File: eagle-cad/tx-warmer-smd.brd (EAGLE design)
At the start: 28.6 x 19 mm, 27 parts, among them Q1 MOSFET-NCHANNELFDS6630A, U2 V_REG_LDOSMD

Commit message: Minor updates to SMD-version
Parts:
- Q1: value MOSFET-NCHANNELFDS6630A -> IR F8721
- U2: value V_REG_LDOSMD -> MCP1804T
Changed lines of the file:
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@@
 <attribute name="VALUE" x="12.827" y="20.574" size="0.4064" layer="25" rot="R90"/>
 </element>
-<element name="Q1" library="SparkFun-DiscreteSemi" package="SO08" value="MOSFET-NCHANNELFDS6630A" x="7.62" y="21.59" smashed="yes">
+<element name="Q1" library="SparkFun-DiscreteSemi" package="SO08" value="IR F8721" x="7.62" y="21.59" smashed="yes">
 <attribute name="PROD_ID" value="IC-08089" x="7.62" y="21.59" size="1.778" layer="27" display="off"/>
 </element>
@@
 <attribute name="VALUE" x="10.287" y="14.224" size="0.4064" layer="25" rot="R90"/>
 </element>
-<element name="U2" library="SparkFun-PowerIC" package="SOT23-5" value="V_REG_LDOSMD" x="10.16" y="11.43" smashed="yes" rot="R270"/>
+<element name="U2" library="SparkFun-PowerIC" package="SOT23-5" value="MCP1804T" x="10.16" y="11.43" smashed="yes" rot="R270"/>
 <element name="S1" library="SparkFun-Electromechanical" package="TACTILE_SWITCH_SMD" value="" x="24.13" y="21.59" smashed="yes">
 <attribute name="PROD_ID" value="SWCH-08247" x="24.13" y="21.59" size="1.778" layer="27" display="off"/>

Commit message: Fixed ldo shutdown-pin and checked values for res/caps
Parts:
- C1, C3: value 2.2uF? -> 1uF
- C2: value 22uF? -> 10uF
- R1: value 270? -> 270
- R5: value 220? -> 220
- R6: value 270? -> 100k
- R8: value 270? -> 33k
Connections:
- net GND: no longer U2.4
- net VIN: now also U2.4
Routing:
- net VIN: track 17.8 -> 21.2 mm
- net GND: vias 0 -> 8
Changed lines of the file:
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@@
 <attribute name="VALUE" x="17.907" y="10.414" size="0.4064" layer="25" rot="R90"/>
 </element>
-<element name="R1" library="SparkFun-Resistors" package="0805" value="270?" x="25.4" y="16.51" smashed="yes" rot="R270">
+<element name="R1" library="SparkFun-Resistors" package="0805" value="270" x="25.4" y="16.51" smashed="yes" rot="R270">
 <attribute name="VALUE" x="24.003" y="17.526" size="0.4064" layer="25" rot="R270"/>
 </element>
-<element name="R5" library="SparkFun-Resistors" package="0805" value="220?" x="22.225" y="16.51" smashed="yes" rot="R270">
+<element name="R5" library="SparkFun-Resistors" package="0805" value="220" x="22.225" y="16.51" smashed="yes" rot="R270">
 <attribute name="VALUE" x="20.828" y="17.526" size="0.4064" layer="25" rot="R270"/>
 </element>
@@
 <attribute name="NAME" x="0.7112" y="22.1488" size="1.016" layer="25" rot="R90"/>
 </element>
-<element name="C3" library="SparkFun-Capacitors" package="0805" value="2.2uF?" x="6.35" y="11.43" smashed="yes" rot="R270">
+<element name="C3" library="SparkFun-Capacitors" package="0805" value="1uF" x="6.35" y="11.43" smashed="yes" rot="R270">
 <attribute name="VALUE" x="5.207" y="10.414" size="0.4064" layer="25" rot="R90"/>
 </element>
-<element name="C1" library="SparkFun-Capacitors" package="0805" value="2.2uF?" x="13.97" y="11.43" smashed="yes" rot="R270">
+<element name="C1" library="SparkFun-Capacitors" package="0805" value="1uF" x="13.97" y="11.43" smashed="yes" rot="R270">
 <attribute name="VALUE" x="12.827" y="10.414" size="0.4064" layer="25" rot="R90"/>
 </element>
-<element name="C2" library="SparkFun-Capacitors" package="0805" value="22uF?" x="16.51" y="11.43" smashed="yes" rot="R270">
+<element name="C2" library="SparkFun-Capacitors" package="0805" value="10uF" x="16.51" y="11.43" smashed="yes" rot="R270">
 <attribute name="VALUE" x="15.367" y="10.414" size="0.4064" layer="25" rot="R90"/>
 </element>
-<element name="R6" library="SparkFun-Resistors" package="0805" value="270?" x="6.35" y="15.24" smashed="yes" rot="R270">
+<element name="R6" library="SparkFun-Resistors" package="0805" value="100k" x="6.35" y="15.24" smashed="yes" rot="R270">
 <attribute name="VALUE" x="5.207" y="14.224" size="0.4064" layer="25" rot="R90"/>
 </element>
-<element name="R8" library="SparkFun-Resistors" package="0805" value="270?" x="8.89" y="15.24" smashed="yes" rot="R90">
+<element name="R8" library="SparkFun-Resistors" package="0805" value="33k" x="8.89" y="15.24" smashed="yes" rot="R90">
 <attribute name="VALUE" x="7.747" y="14.224" size="0.4064" layer="25" rot="R90"/>
 </element>
@@
 <contactref element="R8" pad="1"/>
 <contactref element="C5" pad="2"/>
-<contactref element="U2" pad="4"/>
 <contactref element="U2" pad="2"/>
 <polygon width="0.508" layer="1" isolate="0.3048">
@@
 <vertex x="-1.905" y="6.985"/>
 </polygon>
+<via x="13.97" y="13.97" extent="1-16" drill="0.6"/>
+<via x="10.795" y="19.05" extent="1-16" drill="0.6"/>
+<via x="26.035" y="25.4" extent="1-16" drill="0.6"/>
+<via x="5.08" y="9.525" extent="1-16" drill="0.6"/>
+<via x="7.62" y="9.525" extent="1-16" drill="0.6"/>
+<via x="12.7" y="9.525" extent="1-16" drill="0.6"/>
+<via x="17.78" y="9.525" extent="1-16" drill="0.6"/>
+<via x="23.8125" y="9.525" extent="1-16" drill="0.6"/>
 </signal>
 <signal name="5V">
@@
 <wire x1="6.35" y1="12.7" x2="6.35" y2="13.335" width="0.6096" layer="1"/>
 <wire x1="6.35" y1="13.97" x2="5.715" y2="13.335" width="0.6096" layer="1"/>
+<contactref element="U2" pad="4"/>
+<wire x1="8.8599" y1="12.38" x2="9.21" y2="12.38" width="0.4064" layer="1"/>
+<wire x1="9.21" y1="12.38" x2="11.11" y2="10.48" width="0.4064" layer="1"/>
+<wire x1="11.4601" y1="10.48" x2="11.11" y2="10.48" width="0.4064" layer="1"/>
 </signal>
 <signal name="N$3">

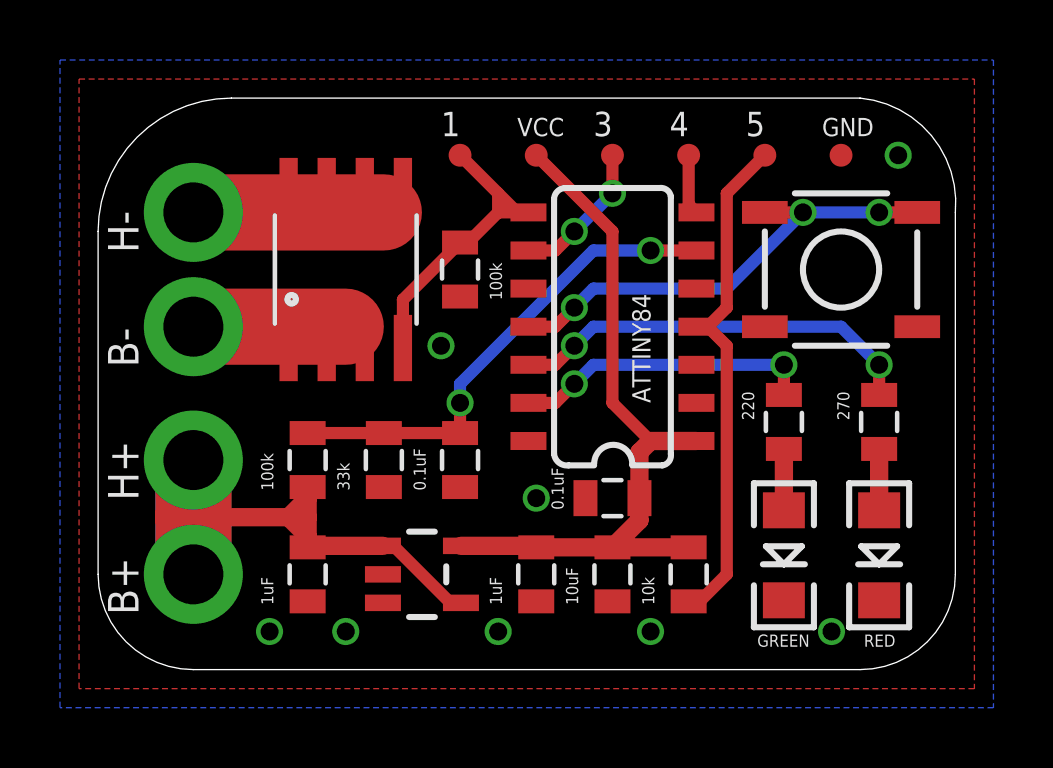
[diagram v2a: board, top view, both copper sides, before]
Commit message: Added top gnd-plane
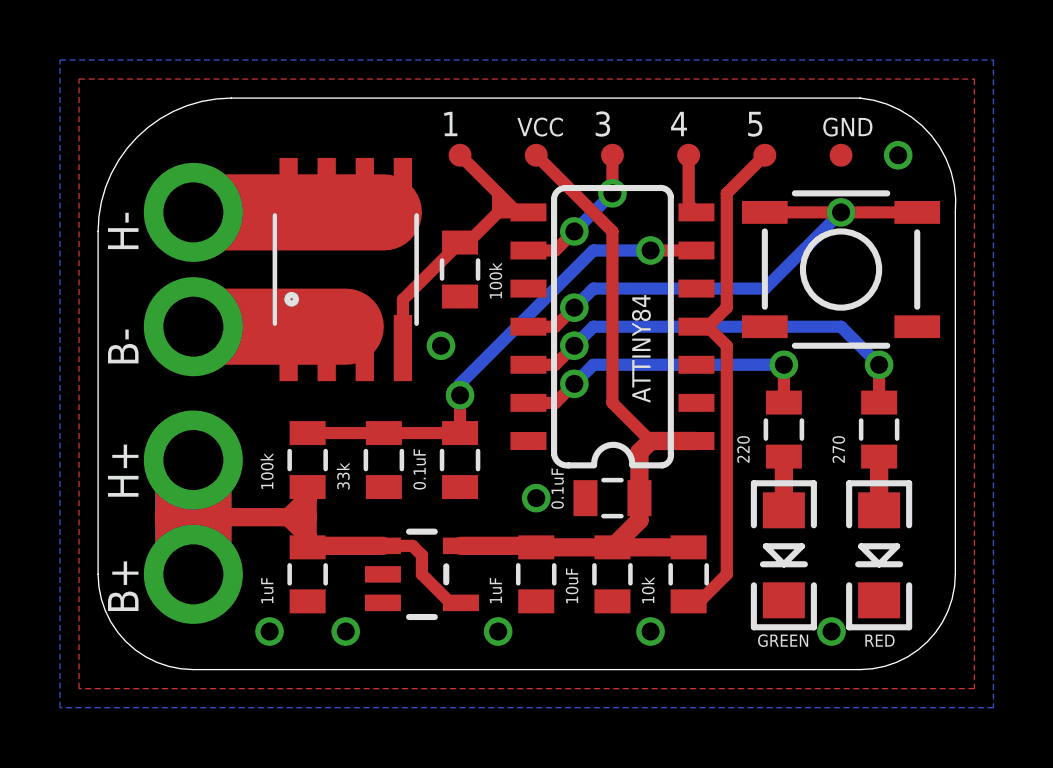
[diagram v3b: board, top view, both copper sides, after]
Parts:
- moved R1 0.25 mm to (25.4, 16.3)
- moved R5 0.25 mm to (22.2, 16.3)
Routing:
- net N$1: track 15.8 -> 17.1 mm, vias 3 -> 2
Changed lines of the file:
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@@
 </class>
 </classes>
-<designrules name="ITEADstudio_DRC">
+<designrules name="LaenPCBOrder">
 <description language="de">&lt;b&gt;EAGLE Design Rules&lt;/b&gt;
 &lt;p&gt;
@@
 Einstellungen hier und speichern die Design Rules unter
 einem neuen Namen ab.</description>
-<description language="en">&lt;b&gt;EAGLE Design Rules&lt;/b&gt;
+<description language="en">&lt;b&gt;Laen's PCB Order Design Rules&lt;/b&gt;
 &lt;p&gt;
-The default Design Rules have been set to cover
-a wide range of applications. Your particular design
-may have different requirements, so please make the
-necessary adjustments and save your customized
-design rules under a new name.</description>
-<description language="zh">&lt;b&gt;Seeed Studio EAGLE Design Rules&lt;/b&gt;
-</description>
+Please make sure your boards conform to these design rules.</description>
 <param name="layerSetup" value="(1*16)"/>
-<param name="mtCopper" value="0.035mm 0.035mm 0.035mm 0.035mm 0.035mm 0.035mm 0.035mm 0.035mm 0.035mm 0.035mm 0.035mm 0.035mm 0.035mm 0.035mm 0.035mm 0.035mm"/>
-<param name="mtIsolate" value="1.5mm 0.15mm 0.2mm 0.15mm 0.2mm 0.15mm 0.2mm 0.15mm 0.2mm 0.15mm 0.2mm 0.15mm 0.2mm 0.15mm 0.2mm"/>
+<param name="mtCopper" value="0.0356mm 0.0356mm 0.0356mm 0.0356mm 0.0356mm 0.0356mm 0.0356mm 0.0356mm 0.0356mm 0.0356mm 0.0356mm 0.0356mm 0.0356mm 0.0356mm 0.0356mm 0.0356mm"/>
+<param name="mtIsolate" value="1.5011mm 0.1499mm 0.2007mm 0.1499mm 0.2007mm 0.1499mm 0.2007mm 0.1499mm 0.2007mm 0.1499mm 0.2007mm 0.1499mm 0.2007mm 0.1499mm 0.2007mm"/>
 <param name="mdWireWire" value="6mil"/>
 <param name="mdWirePad" value="6mil"/>
@@
 <param name="mdPadVia" value="6mil"/>
 <param name="mdViaVia" value="6mil"/>
-<param name="mdSmdPad" value="0mil"/>
-<param name="mdSmdVia" value="0mil"/>
-<param name="mdSmdSmd" value="0mil"/>
+<param name="mdSmdPad" value="6mil"/>
+<param name="mdSmdVia" value="6mil"/>
+<param name="mdSmdSmd" value="6mil"/>
 <param name="mdViaViaSameLayer" value="8mil"/>
 <param name="mnLayersViaInSmd" value="2"/>
-<param name="mdCopperDimension" value="10mil"/>
-<param name="mdDrill" value="10mil"/>
+<param name="mdCopperDimension" value="15mil"/>
+<param name="mdDrill" value="6mil"/>
 <param name="mdSmdStop" value="0mil"/>
 <param name="msWidth" value="6mil"/>
-<param name="msDrill" value="12mil"/>
-<param name="msMicroVia" value="12mil"/>
+<param name="msDrill" value="13mil"/>
+<param name="msMicroVia" value="13mil"/>
 <param name="msBlindViaRatio" value="0.5"/>
 <param name="rvPadTop" value="0.25"/>
@@
 <param name="rvMicroViaOuter" value="0.25"/>
 <param name="rvMicroViaInner" value="0.25"/>
-<param name="rlMinPadTop" value="10mil"/>
+<param name="rlMinPadTop" value="7mil"/>
 <param name="rlMaxPadTop" value="20mil"/>
-<param name="rlMinPadInner" value="10mil"/>
+<param name="rlMinPadInner" value="7mil"/>
 <param name="rlMaxPadInner" value="20mil"/>
-<param name="rlMinPadBottom" value="10mil"/>
+<param name="rlMinPadBottom" value="7mil"/>
 <param name="rlMaxPadBottom" value="20mil"/>
-<param name="rlMinViaOuter" value="6mil"/>
+<param name="rlMinViaOuter" value="7mil"/>
 <param name="rlMaxViaOuter" value="20mil"/>
-<param name="rlMinViaInner" value="6mil"/>
+<param name="rlMinViaInner" value="7mil"/>
 <param name="rlMaxViaInner" value="20mil"/>
 <param name="rlMinMicroViaOuter" value="4mil"/>
@@
 <param name="psTop" value="-1"/>
 <param name="psBottom" value="-1"/>
-<param name="psFirst" value="0"/>
+<param name="psFirst" value="-1"/>
 <param name="psElongationLong" value="100"/>
 <param name="psElongationOffset" value="100"/>
 <param name="mvStopFrame" value="1"/>
 <param name="mvCreamFrame" value="0"/>
-<param name="mlMinStopFrame" value="2mil"/>
-<param name="mlMaxStopFrame" value="2mil"/>
+<param name="mlMinStopFrame" value="4mil"/>
+<param name="mlMaxStopFrame" value="4mil"/>
 <param name="mlMinCreamFrame" value="0mil"/>
 <param name="mlMaxCreamFrame" value="0mil"/>
-<param name="mlViaStopLimit" value="100mil"/>
+<param name="mlViaStopLimit" value="0mil"/>
 <param name="srRoundness" value="0"/>
 <param name="srMinRoundness" value="0mil"/>
@@
 <param name="checkAngle" value="0"/>
 <param name="checkFont" value="1"/>
-<param name="checkRestrict" value="0"/>
+<param name="checkRestrict" value="1"/>
 <param name="useDiameter" value="13"/>
 <param name="maxErrors" value="50"/>
@@
 <attribute name="VALUE" x="17.907" y="10.414" size="0.4064" layer="25" rot="R90"/>
 </element>
-<element name="R1" library="SparkFun-Resistors" package="0805" value="270" x="25.4" y="16.51" smashed="yes" rot="R270">
-<attribute name="VALUE" x="24.003" y="17.526" size="0.4064" layer="25" rot="R270"/>
-</element>
-<element name="R5" library="SparkFun-Resistors" package="0805" value="220" x="22.225" y="16.51" smashed="yes" rot="R270">
-<attribute name="VALUE" x="20.828" y="17.526" size="0.4064" layer="25" rot="R270"/>
+<element name="R1" library="SparkFun-Resistors" package="0805" value="270" x="25.4" y="16.256" smashed="yes" rot="R270">
+<attribute name="VALUE" x="24.257" y="15.113" size="0.4064" layer="25" rot="R90"/>
+</element>
+<element name="R5" library="SparkFun-Resistors" package="0805" value="220" x="22.225" y="16.256" smashed="yes" rot="R270">
+<attribute name="VALUE" x="21.082" y="15.113" size="0.4064" layer="25" rot="R90"/>
 </element>
 <element name="LED3" library="SparkFun-LED" package="LED-1206" value="RED" x="25.4" y="12.065" smashed="yes" rot="R270">
@@
 <via x="25.4" y="18.415" extent="1-16" drill="0.6"/>
 <via x="15.24" y="19.05" extent="1-16" drill="0.6"/>
-<wire x1="25.4" y1="18.415" x2="25.4" y2="17.41" width="0.4064" layer="1"/>
+<wire x1="25.4" y1="18.415" x2="25.4" y2="17.156" width="0.4064" layer="1"/>
 </signal>
 <signal name="N$22">
@@
 <via x="22.225" y="18.415" extent="1-16" drill="0.6"/>
 <via x="15.24" y="17.78" extent="1-16" drill="0.6"/>
-<wire x1="22.225" y1="18.415" x2="22.225" y2="17.41" width="0.4064" layer="1"/>
+<wire x1="22.225" y1="18.415" x2="22.225" y2="17.156" width="0.4064" layer="1"/>
 </signal>
 <signal name="N$24">
 <contactref element="R1" pad="2"/>
 <contactref element="LED3" pad="A"/>
-<wire x1="25.4" y1="15.61" x2="25.4" y2="13.565" width="0.6096" layer="1"/>
+<wire x1="25.4" y1="15.356" x2="25.4" y2="13.565" width="0.6096" layer="1"/>
 </signal>
 <signal name="N$25">
 <contactref element="R5" pad="2"/>
 <contactref element="LED4" pad="A"/>
-<wire x1="22.225" y1="15.61" x2="22.225" y2="13.565" width="0.6096" layer="1"/>
+<wire x1="22.225" y1="15.356" x2="22.225" y2="13.565" width="0.6096" layer="1"/>
 </signal>
 <signal name="N$8">
@@
 <contactref element="S1" pad="2"/>
 <wire x1="15.24" y1="20.32" x2="15.875" y2="20.955" width="0.4064" layer="16"/>
-<wire x1="15.875" y1="20.955" x2="20.32" y2="20.955" width="0.4064" layer="16"/>
-<wire x1="20.32" y1="20.955" x2="22.86" y2="23.495" width="0.4064" layer="16"/>
+<wire x1="15.875" y1="20.955" x2="21.59" y2="20.955" width="0.4064" layer="16"/>
 <wire x1="13.71" y1="19.685" x2="14.605" y2="19.685" width="0.4064" layer="1"/>
 <wire x1="14.605" y1="19.685" x2="15.24" y2="20.32" width="0.4064" layer="1"/>
-<via x="22.86" y="23.495" extent="1-16" drill="0.6"/>
 <via x="15.24" y="20.32" extent="1-16" drill="0.6"/>
-<wire x1="22.86" y1="23.495" x2="21.59" y2="23.495" width="0.4064" layer="1"/>
-<wire x1="22.86" y1="23.495" x2="25.4" y2="23.495" width="0.4064" layer="16"/>
-<via x="25.4" y="23.495" extent="1-16" drill="0.6"/>
-<wire x1="25.4" y1="23.495" x2="26.67" y2="23.495" width="0.4064" layer="1"/>
+<wire x1="21.59" y1="20.955" x2="24.13" y2="23.495" width="0.4064" layer="16"/>
+<via x="24.13" y="23.495" extent="1-16" drill="0.6"/>
+<wire x1="24.13" y1="23.495" x2="26.67" y2="23.495" width="0.4064" layer="1"/>
+<wire x1="24.13" y1="23.495" x2="21.59" y2="23.495" width="0.4064" layer="1"/>
 </signal>
 <signal name="VIN">
@@
 <wire x1="6.35" y1="13.97" x2="5.715" y2="13.335" width="0.6096" layer="1"/>
 <contactref element="U2" pad="4"/>
-<wire x1="8.8599" y1="12.38" x2="9.21" y2="12.38" width="0.4064" layer="1"/>
-<wire x1="9.21" y1="12.38" x2="11.11" y2="10.48" width="0.4064" layer="1"/>
 <wire x1="11.4601" y1="10.48" x2="11.11" y2="10.48" width="0.4064" layer="1"/>
+<wire x1="11.11" y1="10.48" x2="10.16" y2="11.43" width="0.4064" layer="1"/>
+<wire x1="10.16" y1="11.43" x2="10.16" y2="12.065" width="0.4064" layer="1"/>
+<wire x1="8.8599" y1="12.38" x2="9.845" y2="12.38" width="0.4064" layer="1"/>
+<wire x1="9.845" y1="12.38" x2="10.16" y2="12.065" width="0.4064" layer="1"/>
 </signal>
 <signal name="N$3">
@@
 <wire x1="17.78" y1="22.225" x2="15.875" y2="22.225" width="0.4064" layer="16"/>
 <wire x1="15.875" y1="22.225" x2="11.43" y2="17.78" width="0.4064" layer="16"/>
-<wire x1="11.43" y1="17.78" x2="11.43" y2="17.145" width="0.4064" layer="16"/>
-<via x="11.43" y="17.145" extent="1-16" drill="0.6"/>
-<wire x1="11.43" y1="17.145" x2="11.43" y2="16.14" width="0.4064" layer="1"/>
+<wire x1="11.43" y1="17.78" x2="11.43" y2="17.399" width="0.4064" layer="16"/>
+<via x="11.43" y="17.399" extent="1-16" drill="0.6"/>
+<wire x1="11.43" y1="17.399" x2="11.43" y2="16.14" width="0.4064" layer="1"/>
 </signal>
 <signal name="N$4">
